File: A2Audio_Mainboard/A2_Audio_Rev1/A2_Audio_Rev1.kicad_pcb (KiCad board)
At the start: 4 copper layers, 1.2 x 3.8 mm, 213 parts, among them IC1 ES9822QPRO, J1 Battery_Connector, J3 BOOT_JUMPER, J4 12401610E4_2A, J5 104031-0811, J6 SFV15R-1STE1HLF, J7 SJ2-35954B-SMT-TR, SW1 SW_Wuerth_450301014042, SW10 EVQ-PUJ02K, SW11 EVQ-PUJ02K, SW4 SW_Wuerth_450301014042, SW8 EVQ-PUJ02K, SW9 EVQ-PUJ02K, U1 USBLC6-2SC6, U10 OPA1622IDRCR, U11 SI4732-A10-GS, U12 OPA1612AIDR, U13 LT3042xMSE, U14 W25Q16JVSS, U15 CM5108000, U16 AP2112K-3.3, U17 AP2112K-1.8, U18 LT6711A, U19 TPS62130, U2 TPS65987DDHRSHR, U20 AP2112K-1.8, U21 TPS61230DRC, U22 AP2112K-1.2, U23 LTC2954ITS8-1_TRPBF, U24 TPS65131RGE, U25 LT3094xDD, U26 TS5A3159DBVR, U3 TUSB546A-DCIRNQR, U4 BQ25895RTWR, U5 MAX17055ETB_T, U6 U_DAC_L, U7 U_DAC_R, U8 TPS7A2018PDBVR, U9 TPS7A2033PDBVR, Y1 Crystal, Y2 27MHz

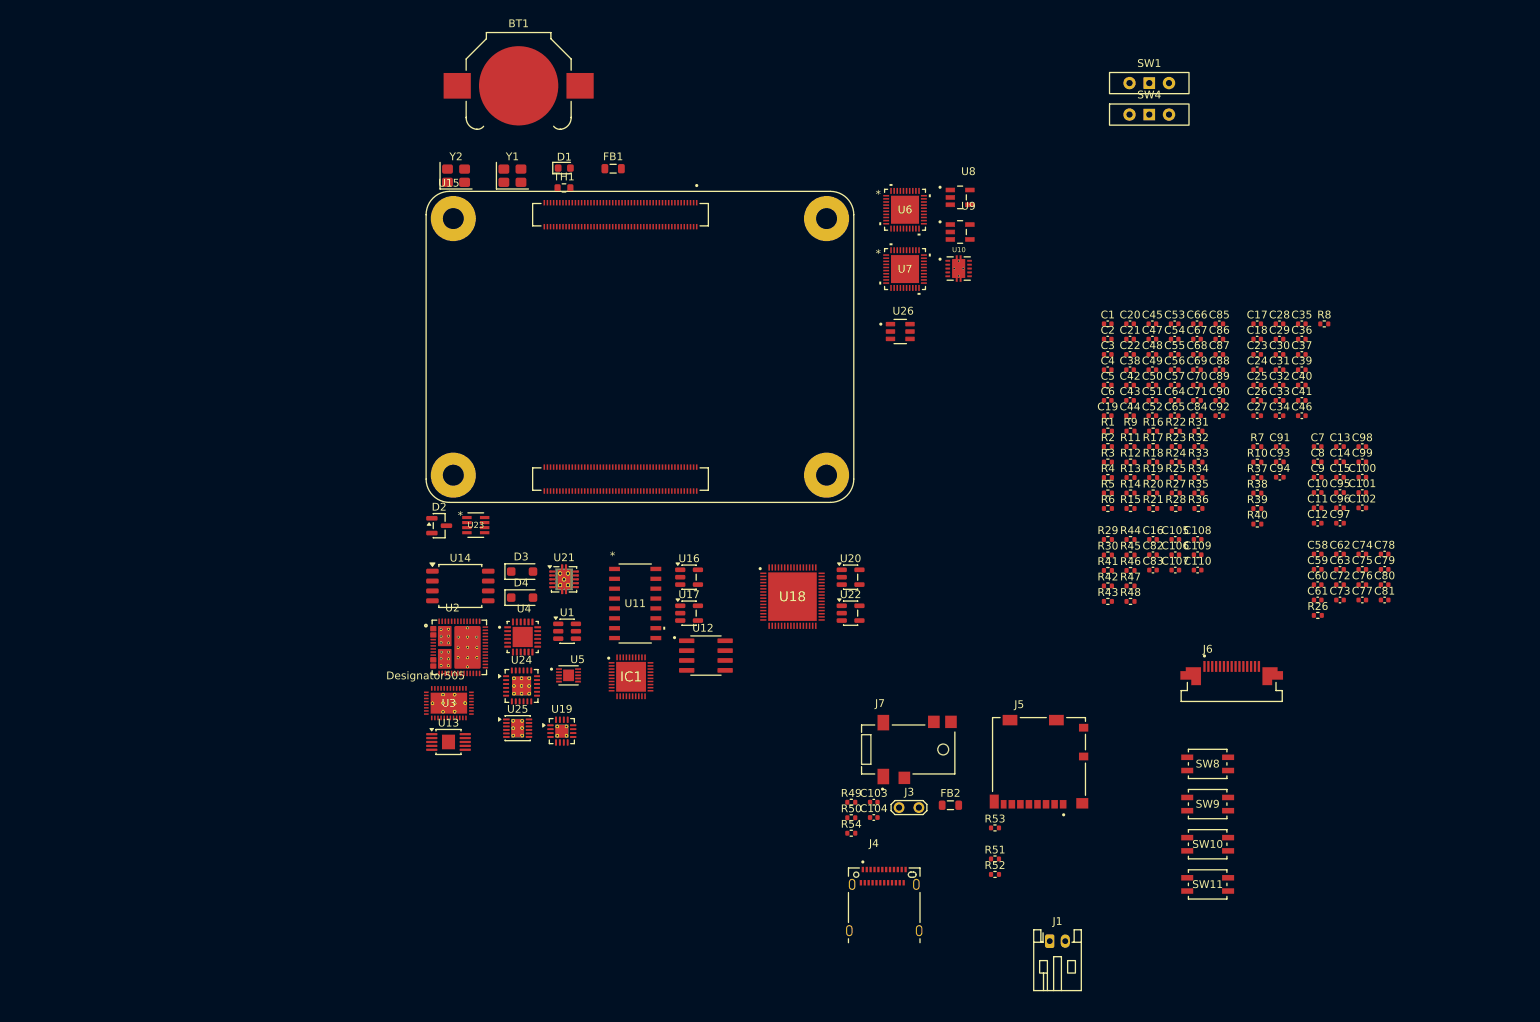
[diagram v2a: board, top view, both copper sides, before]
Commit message: Fixing ERC errors
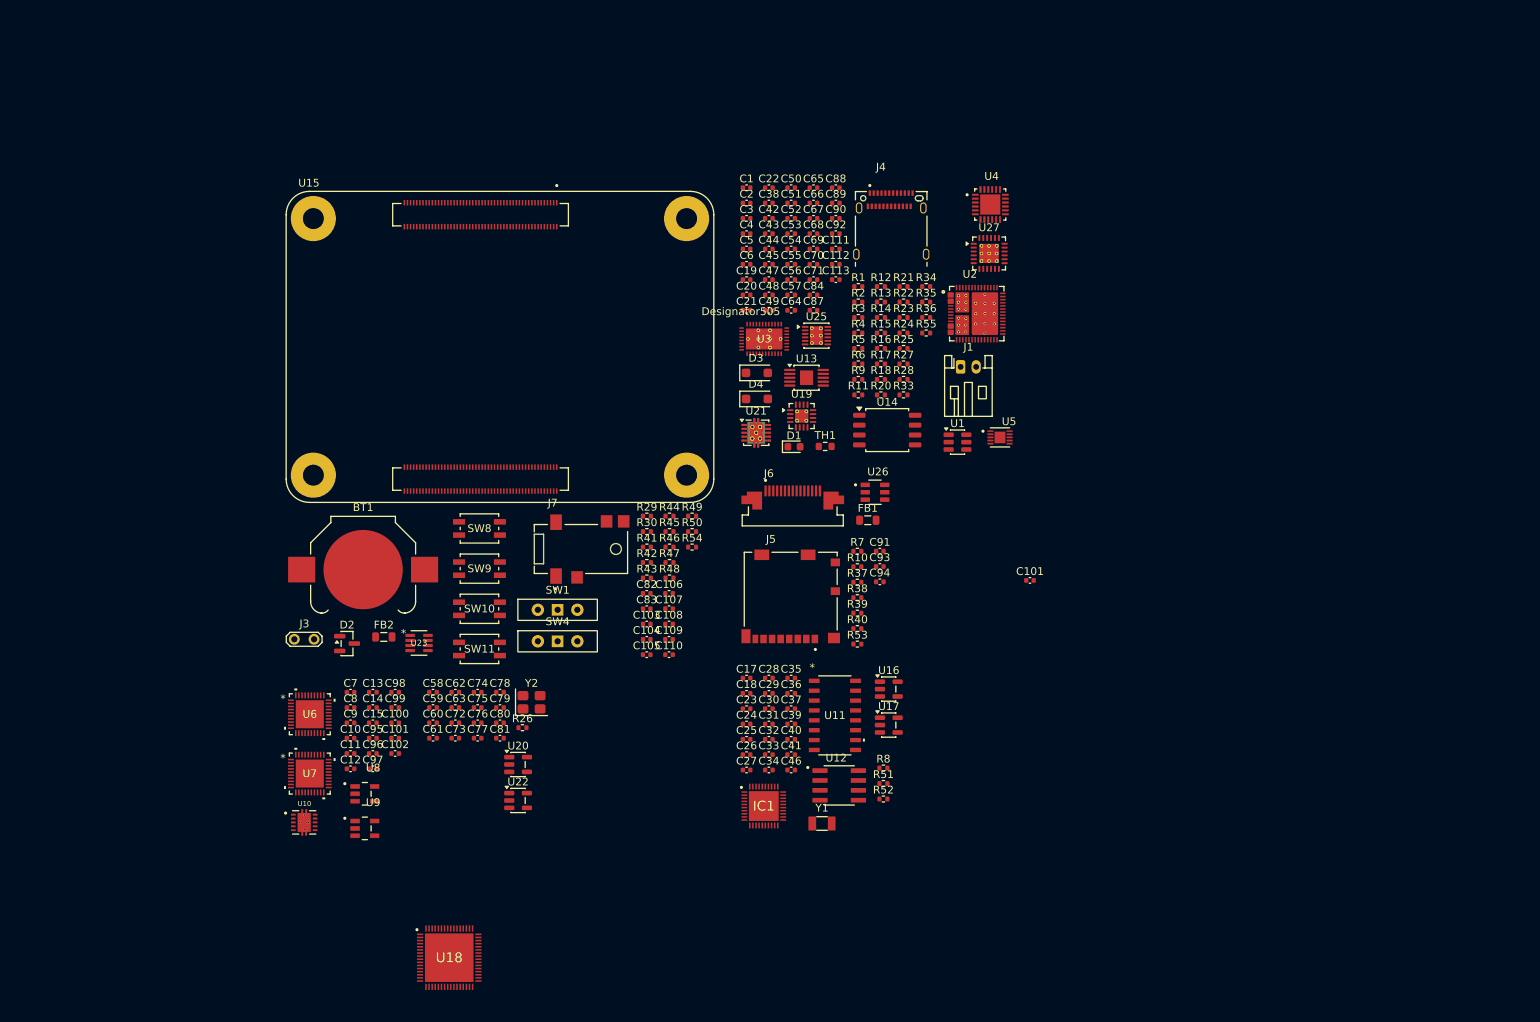
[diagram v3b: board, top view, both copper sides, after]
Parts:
- removed the C101 at (224.7, 90.2)
- removed C16: 33pF, Capacitor_SMD:C_0402_1005Metric
- removed C85: 22µF, Capacitor_SMD:C_0402_1005Metric
- removed C86: 0.22µF, Capacitor_SMD:C_0402_1005Metric
- removed R19: 100kΩ, Resistor_SMD:R_0402_1005Metric
- removed R31: 1MΩ, Resistor_SMD:R_0402_1005Metric
- removed R32: 255kΩ, Resistor_SMD:R_0402_1005Metric
- removed U24: TPS65131RGE, Package_DFN_QFN:VQFN-24-1EP_4x4mm_P0.5mm_EP2.45x2.45mm_ThermalVias
- added C101: 2.2µF, Capacitor_SMD:C_0402_1005Metric, F.Cu at (100.3, 121.8)
- added C101: 100nF, Capacitor_SMD:C_0402_1005Metric, F.Cu at (181.9, 101.5)
- added C111: 4.7µF, Capacitor_SMD:C_0402_1005Metric, F.Cu at (157.0, 58.9)
- added C112: 0.1µF, Capacitor_SMD:C_0402_1005Metric, F.Cu at (157.0, 60.8)
- added C113: 1µF, Capacitor_SMD:C_0402_1005Metric, F.Cu at (157.0, 62.8)
- added R55: 205kΩ, Resistor_SMD:R_0402_1005Metric, F.Cu at (168.6, 69.7)
- added U27: TPS65131RGE, Package_DFN_QFN:VQFN-24-1EP_4x4mm_P0.5mm_EP2.45x2.45mm_ThermalVias, F.Cu at (176.7, 59.4)
- C84: value 22µF -> 4.7µF
- C87: value 4.7nF -> 0.1µF
- C88: value 4.7nF -> 4.7µF
- R28: value 316kΩ -> 23.7kΩ
- R34: value 205kΩ -> 806kΩ
- R36: value 100kΩ -> 806kΩ
- Y1: footprint Crystal:Crystal_SMD_3225-4Pin_3.2x2.5mm -> Crystal:Crystal_SMD_3215-2Pin_3.2x1.5mm
- moved C100 128.3 mm to (100.3, 119.8)
- moved C102 128.3 mm to (100.3, 123.7)
- moved C13 128.3 mm to (97.4, 115.9)
- moved C14 128.3 mm to (97.4, 117.8)
- moved C15 128.3 mm to (97.4, 119.8)
- moved C95 128.3 mm to (97.4, 121.8)
- moved C96 128.3 mm to (97.4, 123.7)
- moved C97 128.3 mm to (97.4, 125.7)
- moved C98 128.3 mm to (100.3, 115.9)
- moved C99 128.3 mm to (100.3, 117.8)
- moved C10 128.3 mm to (94.6, 121.8)
- moved C11 128.3 mm to (94.6, 123.7)
- moved C12 128.3 mm to (94.6, 125.7)
- moved C7 128.3 mm to (94.6, 115.9)
- moved C8 128.3 mm to (94.6, 117.8)
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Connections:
- C22 pad 1: unconnected-(C22-Pad1) -> Net-(U13-SET)
- C22 pad 2: unconnected-(C22-Pad2) -> GND
- C87 pad 1: Net-(C87-Pad1) -> /Power&Battery/+6V_DIRTY
- C88 pad 1: Net-(C88-Pad1) -> Net-(U27-CN)
- C88 pad 2: GND -> Net-(U27-CP)
- C89 pad 1: unconnected-(C89-Pad1) -> Net-(U25-SET)
- C89 pad 2: unconnected-(C89-Pad2) -> GND
- R20 pad 2: Net-(U14-VCC) -> GND
- R33 pad 2: Net-(U24-FBN) -> Net-(U27-FBN)
- R34 pad 1: /Power&Battery/-6V_DIRTY -> Net-(U27-FBN)
- R34 pad 2: Net-(U24-FBN) -> /Power&Battery/-6V_DIRTY
- R35 pad 1: Net-(U24-CP) -> GND
- R35 pad 2: Net-(C87-Pad1) -> Net-(U2-ADCIN2)
- R36 pad 2: Net-(C88-Pad1) -> /Power&Battery/+6V_DIRTY
- U11 pad 8: unconnected-(U11-AMI-Pad8) -> GND
- U14 pad 3: Net-(U14-VCC) -> /+3V3_SYS
- U15 pad 25: /I2S_DATA_OUT -> /I2S_DATA_IN
- U15 pad 27: /I2S_DATA_IN -> /I2S_DATA_OUT
- U2 pad 15: VBUS_A -> /Power&Battery/VBUS_PD
- U2 pad 19: VBUS_A -> /Power&Battery/VBUS_PD
- U2 pad 52: VBUS_A -> /Power&Battery/VBUS_PD
- U2 pad 56: VBUS_A -> /Power&Battery/VBUS_PD
- U2 pad 57: VBUS_A -> /Power&Battery/VBUS_PD
- U2 pad 57_1: VBUS_A -> /Power&Battery/VBUS_PD
- U2 pad 57_2: VBUS_A -> /Power&Battery/VBUS_PD
- U2 pad 57_3: VBUS_A -> /Power&Battery/VBUS_PD
- U2 pad 57_4: VBUS_A -> /Power&Battery/VBUS_PD
- U2 pad 57_5: VBUS_A -> /Power&Battery/VBUS_PD
- U2 pad 57_6: VBUS_A -> /Power&Battery/VBUS_PD
- U2 pad 58: VBUS_A -> /Power&Battery/VBUS_PD
- U2 pad 58_1: VBUS_A -> /Power&Battery/VBUS_PD
- U2 pad 58_2: VBUS_A -> /Power&Battery/VBUS_PD
- U2 pad 58_3: VBUS_A -> /Power&Battery/VBUS_PD
- U2 pad 58_4: VBUS_A -> /Power&Battery/VBUS_PD
- U2 pad 58_5: VBUS_A -> /Power&Battery/VBUS_PD
- U2 pad 58_6: VBUS_A -> /Power&Battery/VBUS_PD
- U2 pad 7: VBUS_A -> /Power&Battery/VBUS_PD
- U2 pad 8: VBUS_A -> /Power&Battery/VBUS_PD
- U25 pad 5: unconnected-(U25-PGFB-Pad5) -> /Power&Battery/-6V_DIRTY
- U25 pad 7: unconnected-(U25-VIOC-Pad7) -> /Power&Battery/-6V_DIRTY
- U3 pad 10: Net-(U3-DP0N) -> /DP_LANE0_N
- U3 pad 12: Net-(U3-DP1P) -> /DP_LANE1_P
- U3 pad 13: Net-(U3-DP1N) -> /DP_LANE1_N
- U3 pad 15: Net-(U3-DP2P) -> /DP_LANE2_P
- U3 pad 16: Net-(U3-DP2N) -> /DP_LANE2_N
- U3 pad 18: Net-(U3-DP3P) -> /DP_LANE3_P
- U3 pad 19: Net-(U3-DP3N) -> /DP_LANE3_N
- U3 pad 9: Net-(U3-DP0P) -> /DP_LANE0_P

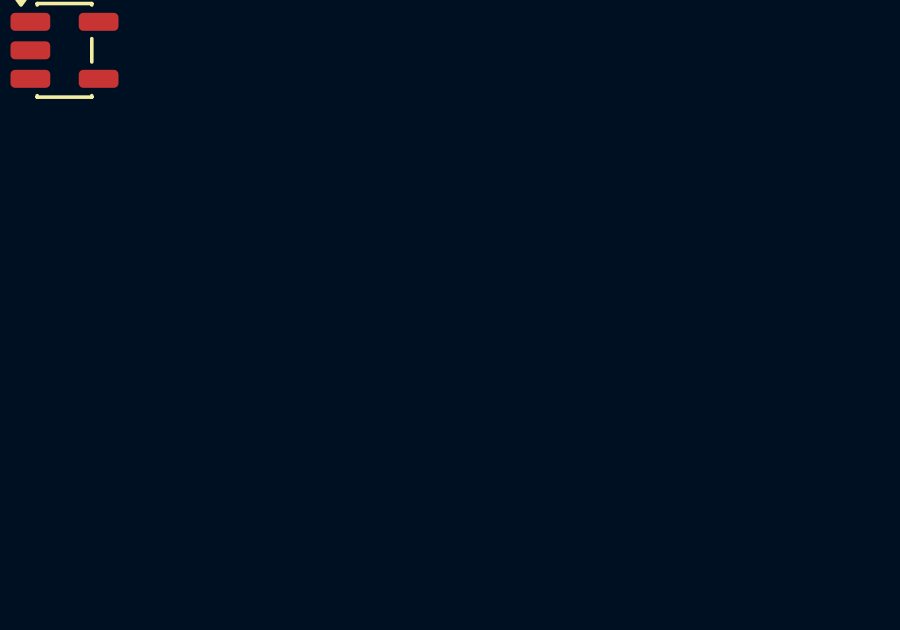
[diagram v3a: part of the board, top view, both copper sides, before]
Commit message: Fixed even more schematic errors
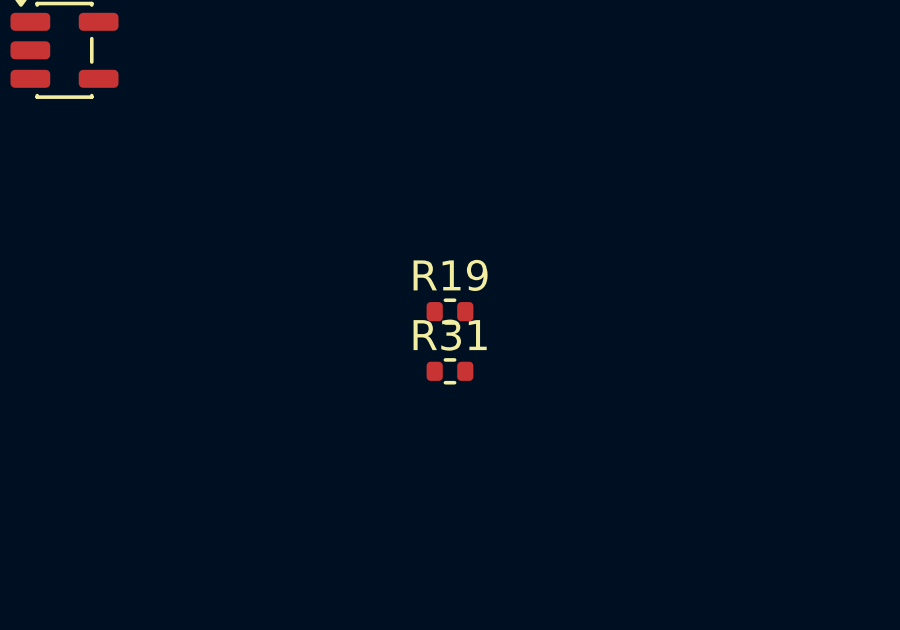
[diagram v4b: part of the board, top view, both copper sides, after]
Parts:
- added R19: 4.7kΩ, Resistor_SMD:R_0402_1005Metric, F.Cu at (129.0, 138.5)
- added R31: 4.7kΩ, Resistor_SMD:R_0402_1005Metric, F.Cu at (129.0, 140.5)
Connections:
- net /+1V8 renamed /Video_Engine/+1V8_VID
- net /+5V_AMP renamed /Recording&Radio_Engine/+5V_AMP
- net /-5V_AMP renamed /Audio_Engine/-5V_AMP
- net /DP_AUX_N renamed /Power&Battery/DP_AUX_N
- net /DP_AUX_P renamed /Power&Battery/DP_AUX_P
- net /DP_HPD renamed /Power&Battery/DP_HPD
- C72 pad 2: /DP_LANE0_P -> /Power&Battery/DP_LANE0_P
- C73 pad 2: /DP_LANE0_N -> /Power&Battery/DP_LANE0_N
- C74 pad 2: /DP_LANE1_P -> /Power&Battery/DP_LANE1_P
- C75 pad 2: /DP_LANE1_N -> /Power&Battery/DP_LANE1_N
- C76 pad 2: /DP_LANE2_P -> /Power&Battery/DP_LANE2_P
- C77 pad 2: /DP_LANE2_N -> /Power&Battery/DP_LANE2_N
- C78 pad 2: /DP_LANE3_P -> /Power&Battery/DP_LANE3_P
- C79 pad 2: /DP_LANE3_N -> /Power&Battery/DP_LANE3_N
- IC1 pad 25: /I2C_SDA -> /I2C_SDA_AUDIO
- IC1 pad 26: /I2C_SCL -> /I2C_SCL_AUDIO
- U15 pad 28: unconnected-(U15A-GPIO13-Pad28) -> /I2C_SCL_AUDIO
- U15 pad 31: /CARD_DETECT -> /I2C_SDA_AUDIO
- U15 pad 37: unconnected-(U15A-GPIO7-Pad37) -> /CARD_DETECT
- U20 pad 2: unconnected-(U20-GND-Pad2) -> GND
- U22 pad 2: unconnected-(U22-GND-Pad2) -> GND
- U3 pad 10: /DP_LANE0_N -> /Power&Battery/DP_LANE0_N
- U3 pad 12: /DP_LANE1_P -> /Power&Battery/DP_LANE1_P
- U3 pad 13: /DP_LANE1_N -> /Power&Battery/DP_LANE1_N
- U3 pad 15: /DP_LANE2_P -> /Power&Battery/DP_LANE2_P
- U3 pad 16: /DP_LANE2_N -> /Power&Battery/DP_LANE2_N
- U3 pad 18: /DP_LANE3_P -> /Power&Battery/DP_LANE3_P
- U3 pad 19: /DP_LANE3_N -> /Power&Battery/DP_LANE3_N
- U3 pad 9: /DP_LANE0_P -> /Power&Battery/DP_LANE0_P
- U6 pad 1: /I2C_SCL -> /I2C_SCL_AUDIO
- U6 pad 39: /I2C_SDA -> /I2C_SDA_AUDIO
- U7 pad 1: /I2C_SCL -> /I2C_SCL_AUDIO
- U7 pad 39: /I2C_SDA -> /I2C_SDA_AUDIO

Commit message: Final touches in schematic
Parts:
- added R32: 22Ω, Resistor_SMD:R_0402_1005Metric, F.Cu at (116.0, 50.5)
- added R56: 22Ω, Resistor_SMD:R_0402_1005Metric, F.Cu at (127.4, 120.0)
- added R57: 22Ω, Resistor_SMD:R_0402_1005Metric, F.Cu at (113.0, 50.5)
- C10, C13: value 2.2µF -> 4.7µF
- R24: value 130Ω -> 180Ω
- R36: value 806kΩ -> 10kΩ
- R55: value 205kΩ -> 31.6kΩ
- moved U15 31.8 mm to (82.0, 69.5)
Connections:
- IC1 pad 8: /I2S_MCLK -> Net-(IC1-XIN)
- J6 pad 14: +5V(INPUT) -> /+3V3_SYS
- J6 pad 15: +5V(INPUT) -> /+3V3_SYS
- U6 pad 37: /I2S_MCLK -> Net-(U6-XTI/MCLK)
- U7 pad 37: /I2S_MCLK -> Net-(U7-XTI/MCLK)
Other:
- board size 1.2 x 3.8 mm -> 194 x 109.5 mm
